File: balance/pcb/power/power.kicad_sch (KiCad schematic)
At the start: 4 parts

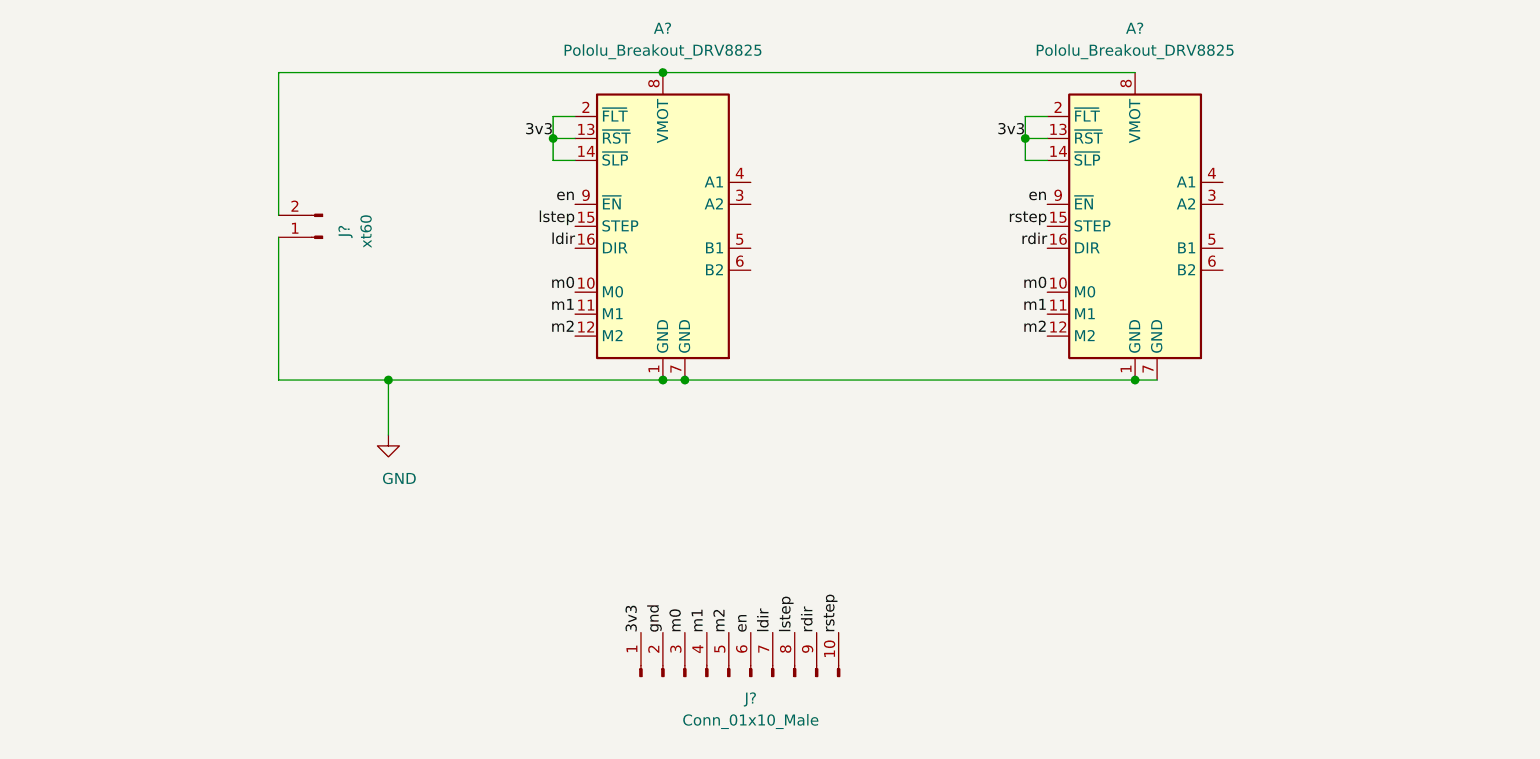
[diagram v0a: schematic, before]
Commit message: balance robot: power board
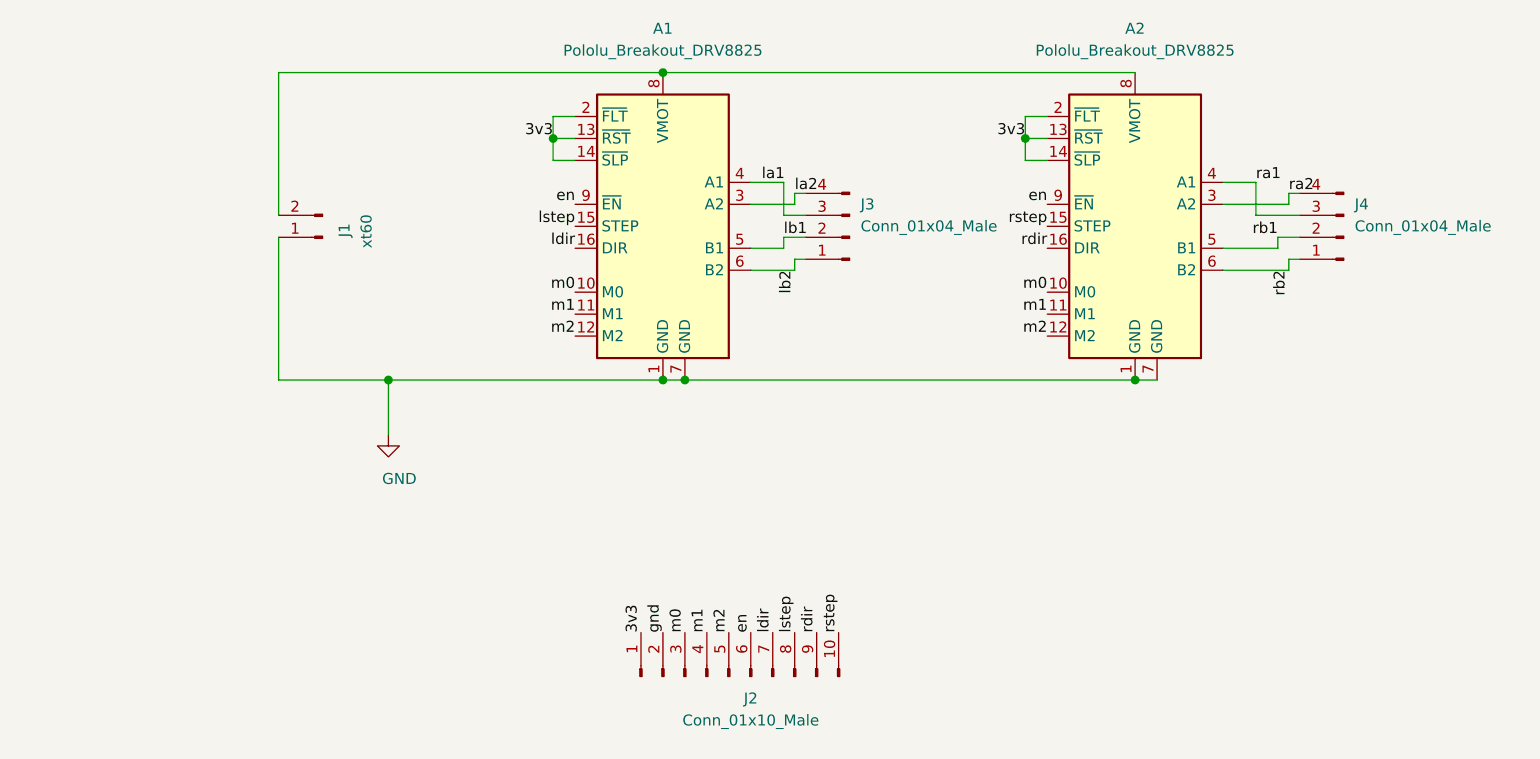
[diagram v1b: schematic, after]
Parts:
- added J3, J4: Conn_01x04_Male, Connector_PinHeader_2.54mm:PinHeader_1x04_P2.54mm_Vertical, symbol Connector:Conn_01x04_Male
- J1: renamed from J?; footprint (none) -> Connector_PinHeader_2.54mm:PinHeader_1x02_P2.54mm_Vertical
- J2: renamed from J?; footprint (none) -> Connector_PinHeader_2.54mm:PinHeader_1x10_P2.54mm_Vertical
- gave numbers to parts that had none: 2
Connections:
- net ra2: now reaches A2.3 (A2)
- net ra2: now also J4.4 (Pin_4)
- net ra1: now reaches A2.4 (A1)
- net ra1: now also J4.3 (Pin_3)
- net rb1: now reaches A2.5 (B1)
- net rb1: now also J4.2 (Pin_2)
- net rb2: now reaches A2.6 (B2)
- net rb2: now also J4.1 (Pin_1)
- net la2: now reaches A1.3 (A2)
- net la2: now also J3.4 (Pin_4)
- net la1: now reaches A1.4 (A1)
- net la1: now also J3.3 (Pin_3)
- net lb1: now reaches A1.5 (B1)
- net lb1: now also J3.2 (Pin_2)
- net lb2: now reaches A1.6 (B2)
- net lb2: now also J3.1 (Pin_1)
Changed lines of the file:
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@@
+    (stroke (width 0) (type solid) (color 0 0 0 0))
+  )
+  (wire (pts (xy 153.67 78.74) (xy 157.48 78.74))
+    (stroke (width 0) (type solid) (color 0 0 0 0))
+  )
+  (wire (pts (xy 153.67 88.9) (xy 158.75 88.9))
+    (stroke (width 0) (type solid) (color 0 0 0 0))
+  )
+  (wire (pts (xy 157.48 82.55) (xy 157.48 78.74))
+    (stroke (width 0) (type solid) (color 0 0 0 0))
+  )
+  (wire (pts (xy 157.48 82.55) (xy 160.02 82.55))
+    (stroke (width 0) (type solid) (color 0 0 0 0))
+  )
+  (wire (pts (xy 157.48 85.09) (xy 157.48 86.36))
+    (stroke (width 0) (type solid) (color 0 0 0 0))
+  )
+  (wire (pts (xy 157.48 86.36) (xy 153.67 86.36))
+    (stroke (width 0) (type solid) (color 0 0 0 0))
+  )
+  (wire (pts (xy 158.75 80.01) (xy 158.75 81.28))
+    (stroke (width 0) (type solid) (color 0 0 0 0))
+  )
+  (wire (pts (xy 158.75 81.28) (xy 153.67 81.28))
+    (stroke (width 0) (type solid) (color 0 0 0 0))
+  )
+  (wire (pts (xy 158.75 87.63) (xy 160.02 87.63))
+    (stroke (width 0) (type solid) (color 0 0 0 0))
+  )
+  (wire (pts (xy 158.75 88.9) (xy 158.75 87.63))
+    (stroke (width 0) (type solid) (color 0 0 0 0))
+  )
+  (wire (pts (xy 160.02 80.01) (xy 158.75 80.01))
+    (stroke (width 0) (type solid) (color 0 0 0 0))
+  )
+  (wire (pts (xy 160.02 85.09) (xy 157.48 85.09))
     (stroke (width 0) (type solid) (color 0 0 0 0))
   )
@@
     (stroke (width 0) (type solid) (color 0 0 0 0))
   )
+  (wire (pts (xy 208.28 88.9) (xy 215.9 88.9))
+    (stroke (width 0) (type solid) (color 0 0 0 0))
+  )
+  (wire (pts (xy 212.09 78.74) (xy 208.28 78.74))
+    (stroke (width 0) (type solid) (color 0 0 0 0))
+  )
+  (wire (pts (xy 212.09 82.55) (xy 212.09 78.74))
+    (stroke (width 0) (type solid) (color 0 0 0 0))
+  )
+  (wire (pts (xy 212.09 82.55) (xy 217.17 82.55))
+    (stroke (width 0) (type solid) (color 0 0 0 0))
+  )
+  (wire (pts (xy 214.63 85.09) (xy 214.63 86.36))
+    (stroke (width 0) (type solid) (color 0 0 0 0))
+  )
+  (wire (pts (xy 214.63 86.36) (xy 208.28 86.36))
+    (stroke (width 0) (type solid) (color 0 0 0 0))
+  )
+  (wire (pts (xy 215.9 80.01) (xy 215.9 81.28))
+    (stroke (width 0) (type solid) (color 0 0 0 0))
+  )
+  (wire (pts (xy 215.9 81.28) (xy 208.28 81.28))
+    (stroke (width 0) (type solid) (color 0 0 0 0))
+  )
+  (wire (pts (xy 215.9 87.63) (xy 217.17 87.63))
+    (stroke (width 0) (type solid) (color 0 0 0 0))
+  )
+  (wire (pts (xy 215.9 88.9) (xy 215.9 87.63))
+    (stroke (width 0) (type solid) (color 0 0 0 0))
+  )
+  (wire (pts (xy 217.17 80.01) (xy 215.9 80.01))
+    (stroke (width 0) (type solid) (color 0 0 0 0))
+  )
+  (wire (pts (xy 217.17 85.09) (xy 214.63 85.09))
+    (stroke (width 0) (type solid) (color 0 0 0 0))
+  )
   (label "3v3" (at 130.81 73.66 180)
     (effects (font (size 1.27 1.27)) (justify right bottom))
@@
     (effects (font (size 1.27 1.27)) (justify left bottom))
   )
+  (label "la1" (at 154.94 78.74 0)
+    (effects (font (size 1.27 1.27)) (justify left bottom))
+  )
   (label "ldir" (at 156.21 130.81 90)
     (effects (font (size 1.27 1.27)) (justify left bottom))
   )
+  (label "lb1" (at 157.48 85.09 0)
+    (effects (font (size 1.27 1.27)) (justify left bottom))
+  )
+  (label "la2" (at 158.75 80.01 0)
+    (effects (font (size 1.27 1.27)) (justify left bottom))
+  )
+  (label "lb2" (at 158.75 88.9 270)
+    (effects (font (size 1.27 1.27)) (justify right bottom))
+  )
   (label "lstep" (at 158.75 130.81 90)
     (effects (font (size 1.27 1.27)) (justify left bottom))
@@
     (effects (font (size 1.27 1.27)) (justify right bottom))
   )
+  (label "ra1" (at 212.09 78.74 0)
+    (effects (font (size 1.27 1.27)) (justify left bottom))
+  )
+  (label "rb1" (at 214.63 85.09 180)
+    (effects (font (size 1.27 1.27)) (justify right bottom))
+  )
+  (label "ra2" (at 215.9 80.01 0)
+    (effects (font (size 1.27 1.27)) (justify left bottom))
+  )
+  (label "rb2" (at 215.9 88.9 270)
+    (effects (font (size 1.27 1.27)) (justify right bottom))
+  )
   (symbol (lib_id "power:GND") (at 111.76 107.95 0) (unit 1)
     (in_bom yes) (on_board yes)
-    (property "Reference" "#PWR?" (id 0) (at 111.76 114.3 0)
+    (property "Reference" "#PWR01" (id 0) (at 111.76 114.3 0)
       (effects (font (size 1.27 1.27)) hide)
     )
@@
   (symbol (lib_id "Connector:Conn_01x02_Male") (at 104.14 85.09 180) (unit 1)
     (in_bom yes) (on_board yes)
-    (property "Reference" "J?" (id 0) (at 106.68 85.09 90)
+    (property "Reference" "J1" (id 0) (at 106.68 85.09 90)
       (effects (font (size 1.27 1.27)) (justify right))
     )
@@
       (effects (font (size 1.27 1.27)) (justify right))
     )
-    (property "Footprint" "" (id 2) (at 104.14 85.09 0)
+    (property "Footprint" "Connector_PinHeader_2.54mm:PinHeader_1x02_P2.54mm_Vertical" (id 2) (at 104.14 85.09 0)
       (effects (font (size 1.27 1.27)) hide)
     )
@@
     )
   )
+  (symbol (lib_id "Connector:Conn_01x04_Male") (at 165.1 85.09 180) (unit 1)
+    (in_bom yes) (on_board yes)
+    (property "Reference" "J3" (id 0) (at 166.37 81.28 0)
+      (effects (font (size 1.27 1.27)) (justify right))
+    )
+    (property "Value" "Conn_01x04_Male" (id 1) (at 166.37 83.82 0)
+      (effects (font (size 1.27 1.27)) (justify right))
+    )
+    (property "Footprint" "Connector_PinHeader_2.54mm:PinHeader_1x04_P2.54mm_Vertical" (id 2) (at 165.1 85.09 0)
+      (effects (font (size 1.27 1.27)) hide)
+    )
+    (property "Datasheet" "~" (id 3) (at 165.1 85.09 0)
+      (effects (font (size 1.27 1.27)) hide)
+    )
+  )
+  (symbol (lib_id "Connector:Conn_01x04_Male") (at 222.25 85.09 180) (unit 1)
+    (in_bom yes) (on_board yes)
+    (property "Reference" "J4" (id 0) (at 223.52 81.28 0)
+      (effects (font (size 1.27 1.27)) (justify right))
+    )
+    (property "Value" "Conn_01x04_Male" (id 1) (at 223.52 83.82 0)
+      (effects (font (size 1.27 1.27)) (justify right))
+    )
+    (property "Footprint" "Connector_PinHeader_2.54mm:PinHeader_1x04_P2.54mm_Vertical" (id 2) (at 222.25 85.09 0)
+      (effects (font (size 1.27 1.27)) hide)
+    )
+    (property "Datasheet" "~" (id 3) (at 222.25 85.09 0)
+      (effects (font (size 1.27 1.27)) hide)
+    )
+  )
   (symbol (lib_id "Connector:Conn_01x10_Male") (at 151.13 135.89 90) (unit 1)
     (in_bom yes) (on_board yes)
-    (property "Reference" "J?" (id 0) (at 153.67 138.43 90))
+    (property "Reference" "J2" (id 0) (at 153.67 138.43 90))
     (property "Value" "Conn_01x10_Male" (id 1) (at 153.67 140.97 90))
-    (property "Footprint" "" (id 2) (at 151.13 135.89 0)
+    (property "Footprint" "Connector_PinHeader_2.54mm:PinHeader_1x10_P2.54mm_Vertical" (id 2) (at 151.13 135.89 0)
       (effects (font (size 1.27 1.27)) hide)
     )
@@
   (symbol (lib_id "Driver_Motor:Pololu_Breakout_DRV8825") (at 143.51 81.28 0) (unit 1)
     (in_bom yes) (on_board yes)
-    (property "Reference" "A?" (id 0) (at 143.51 60.96 0))
+    (property "Reference" "A1" (id 0) (at 143.51 60.96 0))
     (property "Value" "Pololu_Breakout_DRV8825" (id 1) (at 143.51 63.5 0))
     (property "Footprint" "Module:Pololu_Breakout-16_15.2x20.3mm" (id 2) (at 148.59 101.6 0)
@@
   (symbol (lib_id "Driver_Motor:Pololu_Breakout_DRV8825") (at 198.12 81.28 0) (unit 1)
     (in_bom yes) (on_board yes)
-    (property "Reference" "A?" (id 0) (at 198.12 60.96 0))
+    (property "Reference" "A2" (id 0) (at 198.12 60.96 0))
     (property "Value" "Pololu_Breakout_DRV8825" (id 1) (at 198.12 63.5 0))
     (property "Footprint" "Module:Pololu_Breakout-16_15.2x20.3mm" (id 2) (at 203.2 101.6 0)
@@
   (symbol_instances
     (path "/54c3a369-0bf8-46d2-a6af-02bc3649aed4"
-      (reference "#PWR?") (unit 1) (value "GND") (footprint "")
+      (reference "#PWR01") (unit 1) (value "GND") (footprint "")
+    )
+    (path "/bf039d62-1e84-43da-98b4-19fea9d358e6"
+      (reference "A1") (unit 1) (value "Pololu_Breakout_DRV8825") (footprint "Module:Pololu_Breakout-16_15.2x20.3mm")
     )
     (path "/af056bd6-7080-47e0-afae-c5d125dd7284"
-      (reference "A?") (unit 1) (value "Pololu_Breakout_DRV8825") (footprint "Module:Pololu_Breakout-16_15.2x20.3mm")
-    )
-    (path "/bf039d62-1e84-43da-98b4-19fea9d358e6"
-      (reference "A?") (unit 1) (value "Pololu_Breakout_DRV8825") (footprint "Module:Pololu_Breakout-16_15.2x20.3mm")
+      (reference "A2") (unit 1) (value "Pololu_Breakout_DRV8825") (footprint "Module:Pololu_Breakout-16_15.2x20.3mm")
+    )
+    (path "/8c624431-9702-4f63-bb78-ff91d94e08f9"
+      (reference "J1") (unit 1) (value "xt60") (footprint "Connector_PinHeader_2.54mm:PinHeader_1x02_P2.54mm_Vertical")
     )
     (path "/097ce757-7e09-4561-bb91-ea3863338f86"
-      (reference "J?") (unit 1) (value "Conn_01x10_Male") (footprint "")
-    )
-    (path "/8c624431-9702-4f63-bb78-ff91d94e08f9"
-      (reference "J?") (unit 1) (value "xt60") (footprint "")
-    )
-  )
+      (reference "J2") (unit 1) (value "Conn_01x10_Male") (footprint "Connector_PinHeader_2.54mm:PinHeader_1x10_P2.54mm_Vertical")
+    )
+    (path "/632b8139-b5b2-40d1-99c4-7eb921a8cc10"
+      (reference "J3") (unit 1) (value "Conn_01x04_Male") (footprint "Connector_PinHeader_2.54mm:PinHeader_1x04_P2.54mm_Vertical")
+    )
+    (path "/11843d08-b621-4feb-8064-e4d7204368f4"
+      (reference "J4") (unit 1) (value "Conn_01x04_Male") (footprint "Connector_PinHeader_2.54mm:PinHeader_1x04_P2.54mm_Vertical")
+    )
+  )

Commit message: balance robot: power board
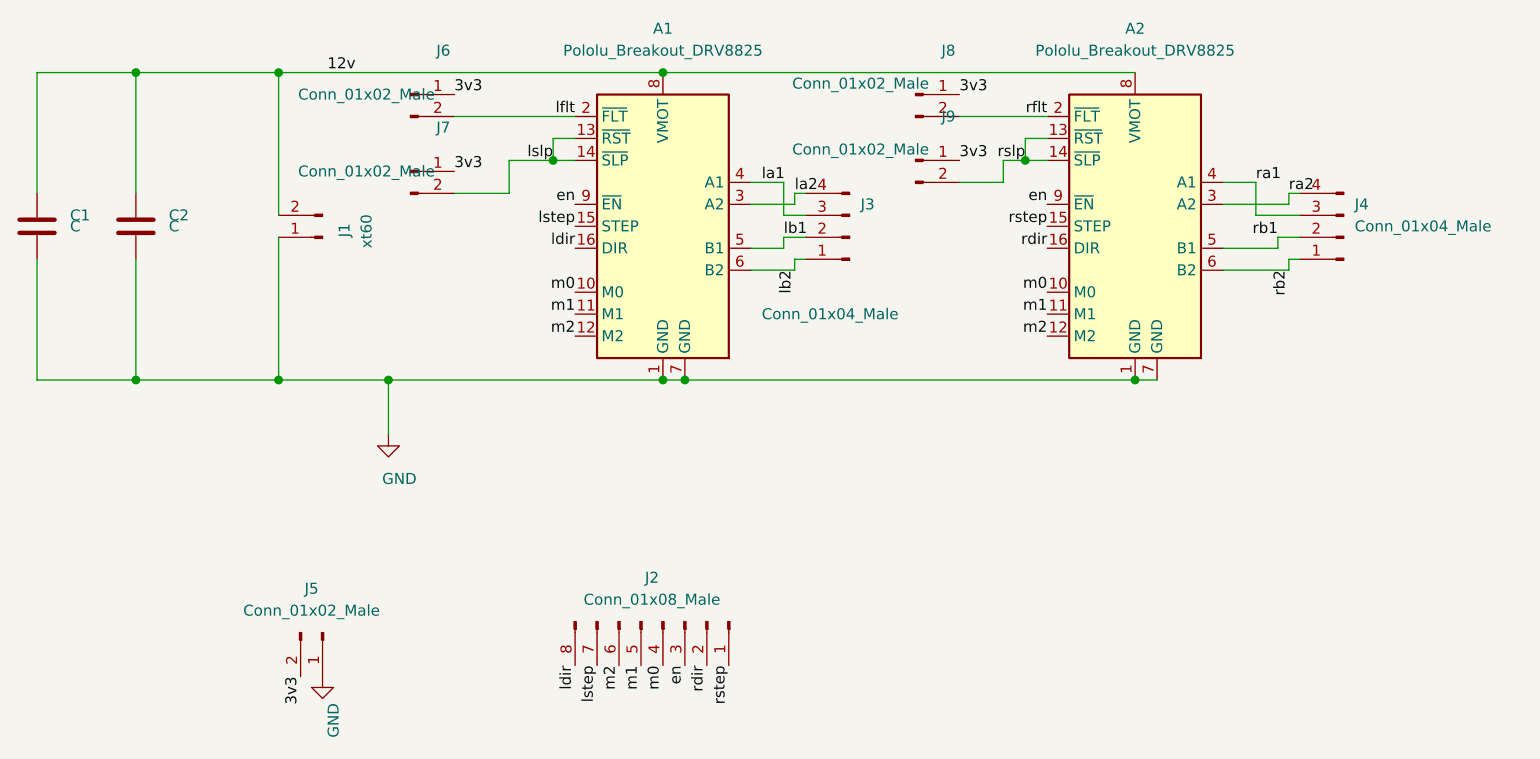
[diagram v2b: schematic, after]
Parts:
- removed J2: Conn_01x10_Male, Connector_PinHeader_2.54mm:PinHeader_1x10_P2.54mm_Vertical, symbol Connector:Conn_01x10_Male
- added C1, C2: C, Capacitor_THT:CP_Radial_D8.0mm_P2.50mm, symbol Device:C
- added J2: Conn_01x08_Male, Connector_PinHeader_2.54mm:PinHeader_1x08_P2.54mm_Vertical, symbol Connector:Conn_01x08_Male
- added J5, J6, J7, J8, J9: Conn_01x02_Male, Connector_PinHeader_2.54mm:PinHeader_1x02_P2.54mm_Vertical, symbol Connector:Conn_01x02_Male
- J1: footprint Connector_PinHeader_2.54mm:PinHeader_1x02_P2.54mm_Vertical -> Connector_AMASS:AMASS_XT60-M_1x02_P7.20mm_Vertical
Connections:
- net 3v3: now also J5.2 (Pin_2), J6.1 (Pin_1), J7.1 (Pin_1), J8.1 (Pin_1), J9.1 (Pin_1); no longer A1.13 (~RST), A1.14 (~SLP), A1.2 (~FLT), A2.13 (~RST), A2.14 (~SLP), A2.2 (~FLT)
- net GND: now also C1.2, C2.2, J5.1 (Pin_1)
- net en: now also J2.3 (Pin_3)
- net ldir: now also J2.8 (Pin_8)
- net lstep: now also J2.7 (Pin_7)
- net m0: now also J2.4 (Pin_4)
- net m1: now also J2.5 (Pin_5)
- net m2: now also J2.6 (Pin_6)
- net rdir: now also J2.2 (Pin_2)
- net rstep: now also J2.1 (Pin_1)
- net 12v: now reaches A1.8 (VMOT), A2.8 (VMOT), J1.2 (Pin_2)
- net 12v: now also C1.1, C2.1
- new net lflt: A1.2 (~FLT), J6.2 (Pin_2)
- new net lslp: A1.13 (~RST), A1.14 (~SLP), J7.2 (Pin_2)
- new net rflt: A2.2 (~FLT), J8.2 (Pin_2)
- new net rslp: A2.13 (~RST), A2.14 (~SLP), J9.2 (Pin_2)
